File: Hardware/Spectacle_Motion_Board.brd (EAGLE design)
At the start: 25.4 x 55.9 mm, 49 parts, among them J10 AUDIO-JACK3, J3 USB-MICROB, J4 AUDIO-JACK3, U1 CY8C4146LQI-S422, U2 3.3V/150mA, U4 SN74LVC1G66, U5 SN74LVC1G66

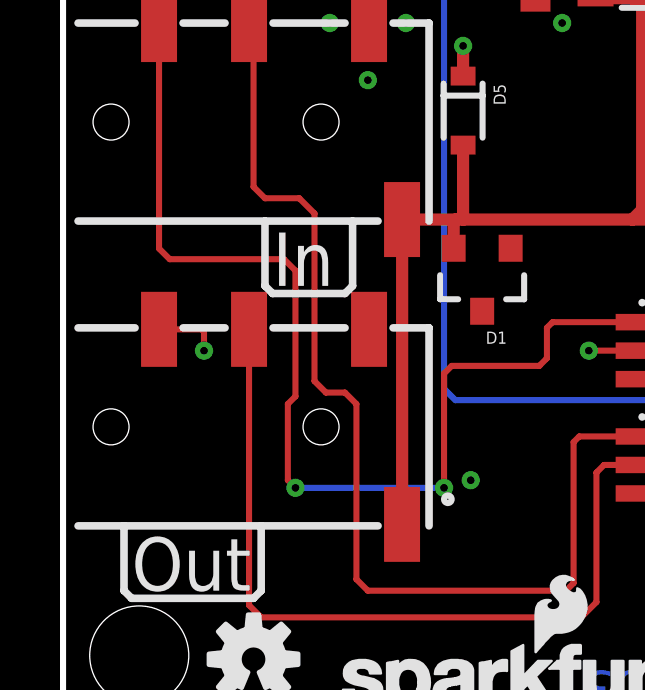
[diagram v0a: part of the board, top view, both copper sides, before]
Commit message: Added and fixed some product IDs
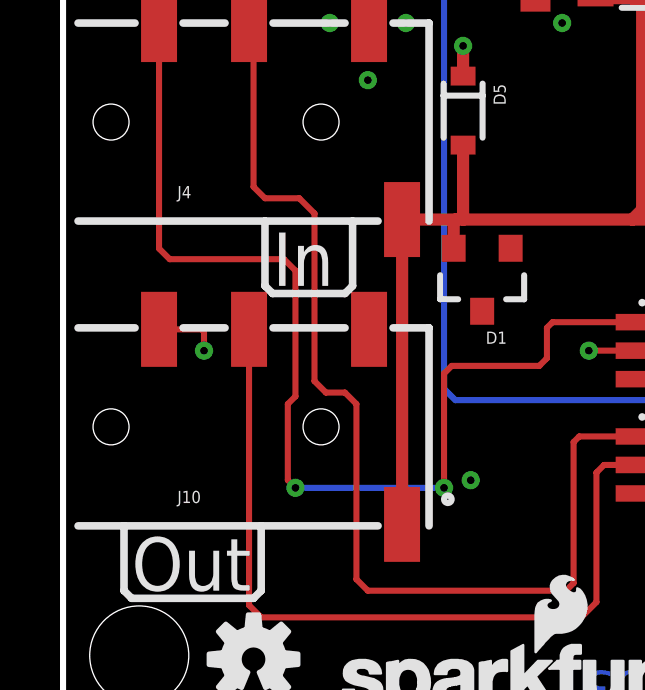
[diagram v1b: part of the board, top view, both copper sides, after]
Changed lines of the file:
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@@
 <grid distance="0.05" unitdist="inch" unit="inch" style="lines" multiple="1" display="yes" altdistance="0.005" altunitdist="inch" altunit="inch"/>
 <layers>
-<layer number="1" name="Top" color="4" fill="1" visible="no" active="yes"/>
+<layer number="1" name="Top" color="4" fill="1" visible="yes" active="yes"/>
 <layer number="2" name="Route2" color="1" fill="3" visible="no" active="yes"/>
-<layer number="15" name="Route15" color="4" fill="6" visible="yes" active="yes"/>
-<layer number="16" name="Bottom" color="1" fill="1" visible="no" active="yes"/>
+<layer number="15" name="Route15" color="4" fill="6" visible="no" active="yes"/>
+<layer number="16" name="Bottom" color="1" fill="1" visible="yes" active="yes"/>
 <layer number="17" name="Pads" color="2" fill="1" visible="yes" active="yes"/>
 <layer number="18" name="Vias" color="2" fill="1" visible="yes" active="yes"/>
 <layer number="19" name="Unrouted" color="6" fill="1" visible="yes" active="yes"/>
 <layer number="20" name="Dimension" color="15" fill="1" visible="yes" active="yes"/>
-<layer number="21" name="tPlace" color="16" fill="1" visible="no" active="yes"/>
-<layer number="22" name="bPlace" color="14" fill="1" visible="no" active="yes"/>
-<layer number="23" name="tOrigins" color="15" fill="1" visible="no" active="yes"/>
-<layer number="24" name="bOrigins" color="15" fill="1" visible="no" active="yes"/>
+<layer number="21" name="tPlace" color="16" fill="1" visible="yes" active="yes"/>
+<layer number="22" name="bPlace" color="14" fill="1" visible="yes" active="yes"/>
+<layer number="23" name="tOrigins" color="15" fill="1" visible="yes" active="yes"/>
+<layer number="24" name="bOrigins" color="15" fill="1" visible="yes" active="yes"/>
 <layer number="25" name="tNames" color="7" fill="1" visible="no" active="yes"/>
 <layer number="26" name="bNames" color="7" fill="1" visible="no" active="yes"/>
@@
 <layer number="43" name="vRestrict" color="2" fill="10" visible="no" active="yes"/>
 <layer number="44" name="Drills" color="7" fill="1" visible="no" active="yes"/>
-<layer number="45" name="Holes" color="7" fill="1" visible="no" active="yes"/>
+<layer number="45" name="Holes" color="7" fill="1" visible="yes" active="yes"/>
 <layer number="46" name="Milling" color="3" fill="1" visible="no" active="yes"/>
 <layer number="47" name="Measures" color="7" fill="1" visible="no" active="yes"/>
 <layer number="48" name="Document" color="7" fill="1" visible="no" active="yes"/>
 <layer number="49" name="Reference" color="7" fill="1" visible="no" active="yes"/>
-<layer number="51" name="tDocu" color="6" fill="1" visible="no" active="yes"/>
+<layer number="51" name="tDocu" color="6" fill="1" visible="yes" active="yes"/>
 <layer number="52" name="bDocu" color="7" fill="1" visible="no" active="yes"/>
 <layer number="3" name="Route3" color="4" fill="3" visible="no" active="no"/>
@@
 <element name="H3" library="SparkFun-Electromechanical" package="STAND-OFF" value="STAND-OFF" x="22.86" y="2.54"/>
 <element name="H4" library="SparkFun-Electromechanical" package="STAND-OFF" value="STAND-OFF" x="2.54" y="2.54"/>
-<element name="J3" library="SparkFun-Connectors" package="USB-B-MICRO-SMD_V03_RED_PASTE" value="USB-MICROB" x="12.7" y="53.848" rot="R270"/>
-<element name="J5" library="SparkFun-Connectors" package="1X03_LOCK" value="" x="6.35" y="41.91" rot="R90"/>
-<element name="J6" library="SparkFun-Connectors" package="1X03_LOCK" value="" x="9.525" y="41.91" rot="R90"/>
-<element name="J7" library="SparkFun-Connectors" package="1X03_LOCK" value="" x="12.7" y="41.91" rot="R90"/>
-<element name="J8" library="SparkFun-Connectors" package="1X03_LOCK" value="" x="15.875" y="41.91" rot="R90"/>
-<element name="J9" library="SparkFun-Connectors" package="1X03_LOCK" value="" x="19.05" y="41.91" rot="R90"/>
+<element name="J3" library="SparkFun-Connectors" package="USB-B-MICRO-SMD_V03_RED_PASTE" value="USB-MICROB" x="12.7" y="53.848" rot="R270">
+<attribute name="PROD_ID" value="CONN-11752" x="12.7" y="53.848" size="1.778" layer="27" rot="R270" display="off"/>
+</element>
+<element name="J5" library="SparkFun-Connectors" package="1X03_LOCK" value="" x="6.35" y="41.91" rot="R90">
+<attribute name="PROD_ID" value="CONN-09692" x="6.35" y="41.91" size="1.778" layer="27" rot="R90" display="off"/>
+</element>
+<element name="J6" library="SparkFun-Connectors" package="1X03_LOCK" value="" x="9.525" y="41.91" rot="R90">
+<attribute name="PROD_ID" value="CONN-09692" x="9.525" y="41.91" size="1.778" layer="27" rot="R90" display="off"/>
+</element>
+<element name="J7" library="SparkFun-Connectors" package="1X03_LOCK" value="" x="12.7" y="41.91" rot="R90">
+<attribute name="PROD_ID" value="CONN-09692" x="12.7" y="41.91" size="1.778" layer="27" rot="R90" display="off"/>
+</element>
+<element name="J8" library="SparkFun-Connectors" package="1X03_LOCK" value="" x="15.875" y="41.91" rot="R90">
+<attribute name="PROD_ID" value="CONN-09692" x="15.875" y="41.91" size="1.778" layer="27" rot="R90" display="off"/>
+</element>
+<element name="J9" library="SparkFun-Connectors" package="1X03_LOCK" value="" x="19.05" y="41.91" rot="R90">
+<attribute name="PROD_ID" value="CONN-09692" x="19.05" y="41.91" size="1.778" layer="27" rot="R90" display="off"/>
+</element>
 <element name="U$1" library="SparkFun-Aesthetics" package="FOUR_LAYER_WARNING" value="FOUR_LAYER_WARNING" x="39.37" y="54.61"/>
 <element name="LOGO1" library="SparkFun-Aesthetics" package="OSHW-LOGO-S" value="OSHW-LOGOS" x="6.35" y="2.413"/>
@@
 <attribute name="PROD_ID" value="DIO-11623" x="13.335" y="20.701" size="1.778" layer="27" font="vector" ratio="15" rot="R270" display="off"/>
 </element>
-<element name="J11" library="SparkFun-Connectors" package="1X06_NO_SILK" value="" x="1.27" y="43.18" rot="R270">
-<attribute name="PROD_ID" value="CONN-08437" x="1.27" y="43.18" size="1.778" layer="27" font="vector" ratio="15" rot="R270" display="off"/>
-</element>
+<element name="J11" library="SparkFun-Connectors" package="1X06_NO_SILK" value="" x="1.27" y="43.18" rot="R270"/>
 <element name="U4" library="SparkFun-AnalogIC" package="SOT23-5" value="SN74LVC1G66" x="20.32" y="12.7" rot="R270">
 <attribute name="PROD_ID" value="IC-13549" x="25.4" y="17.78" size="1.778" layer="27" font="vector" ratio="15" rot="R270" display="off"/>

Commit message: Touchups for v10
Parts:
- J10, J4: value AUDIO-JACK3 -> TRRS_3.5mm; device SparkFun-Connectors:AUDIO-JACK-TRRS-SMD -> SparkFun-Connectors:AUDIO_JACK_3.5MM_TRRS_SMD_RA
- moved LOGO3 18.7 mm to (19.4, 5.71)
- moved LOGO4 1.27 mm to (2.16, 46.6)
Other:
- board text added: "v10"
- board text removed: "v03"
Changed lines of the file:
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@@
 <?xml version="1.0" encoding="utf-8"?>
 <!DOCTYPE eagle SYSTEM "eagle.dtd">
-<eagle version="7.6.0">
+<eagle version="7.7.0">
 <drawing>
 <settings>
@@
 <grid distance="0.05" unitdist="inch" unit="inch" style="lines" multiple="1" display="yes" altdistance="0.005" altunitdist="inch" altunit="inch"/>
 <layers>
-<layer number="1" name="Top" color="4" fill="1" visible="yes" active="yes"/>
+<layer number="1" name="Top" color="4" fill="1" visible="no" active="yes"/>
 <layer number="2" name="Route2" color="1" fill="3" visible="no" active="yes"/>
 <layer number="15" name="Route15" color="4" fill="6" visible="no" active="yes"/>
@@
 <layer number="19" name="Unrouted" color="6" fill="1" visible="yes" active="yes"/>
 <layer number="20" name="Dimension" color="15" fill="1" visible="yes" active="yes"/>
-<layer number="21" name="tPlace" color="16" fill="1" visible="yes" active="yes"/>
+<layer number="21" name="tPlace" color="16" fill="1" visible="no" active="yes"/>
 <layer number="22" name="bPlace" color="14" fill="1" visible="yes" active="yes"/>
-<layer number="23" name="tOrigins" color="15" fill="1" visible="yes" active="yes"/>
+<layer number="23" name="tOrigins" color="15" fill="1" visible="no" active="yes"/>
 <layer number="24" name="bOrigins" color="15" fill="1" visible="yes" active="yes"/>
 <layer number="25" name="tNames" color="7" fill="1" visible="no" active="yes"/>
@@
 <layer number="43" name="vRestrict" color="2" fill="10" visible="no" active="yes"/>
 <layer number="44" name="Drills" color="7" fill="1" visible="no" active="yes"/>
-<layer number="45" name="Holes" color="7" fill="1" visible="yes" active="yes"/>
+<layer number="45" name="Holes" color="7" fill="1" visible="no" active="yes"/>
 <layer number="46" name="Milling" color="3" fill="1" visible="no" active="yes"/>
 <layer number="47" name="Measures" color="7" fill="1" visible="no" active="yes"/>
 <layer number="48" name="Document" color="7" fill="1" visible="no" active="yes"/>
 <layer number="49" name="Reference" color="7" fill="1" visible="no" active="yes"/>
-<layer number="51" name="tDocu" color="6" fill="1" visible="yes" active="yes"/>
+<layer number="51" name="tDocu" color="6" fill="1" visible="no" active="yes"/>
 <layer number="52" name="bDocu" color="7" fill="1" visible="no" active="yes"/>
 <layer number="3" name="Route3" color="4" fill="3" visible="no" active="no"/>
@@
 <text x="19.177" y="49.149" size="1.4224" layer="21" font="vector" ratio="15" align="center">4</text>
 <text x="90.17" y="45.72" size="1.778" layer="51" font="vector" ratio="15">Mike Hord</text>
-<text x="20.32" y="0.762" size="1.27" layer="16" font="vector" ratio="15" rot="MR0">v03</text>
+<text x="20.32" y="0.762" size="1.27" layer="16" font="vector" ratio="15" rot="MR0">v10</text>
 <text x="0.635" y="50.038" size="1.27" layer="1" font="vector" ratio="15">1</text>
 <text x="1.778" y="50.038" size="1.27" layer="2" font="vector" ratio="15">2</text>
@@
 <wire x1="9.398" y1="14.605" x2="9.652" y2="14.859" width="0.254" layer="21"/>
 <wire x1="9.652" y1="14.859" x2="9.652" y2="17.018" width="0.254" layer="21"/>
-<circle x="12.827" y="7.747" radius="0.127" width="0.2032" layer="21"/>
 </plain>
 <attributes>
@@
 <attribute name="PROD_ID" value="RES-07856" x="19.05" y="30.48" size="1.778" layer="27" font="vector" ratio="15" rot="R180" display="off"/>
 </element>
-<element name="J4" library="SparkFun-Connectors" package="AUDIO-JACK-TRRS-SMD" value="AUDIO-JACK3" x="0" y="20.32">
+<element name="J4" library="SparkFun-Connectors" package="AUDIO_JACK_3.5MM_TRRS_SMD_RA" value="TRRS_3.5mm" x="0" y="20.32">
 <attribute name="PROD_ID" value="CONN-10676" x="0" y="20.32" size="1.778" layer="27" display="off"/>
+<attribute name="SF_ID" value="PRT-12639" x="0" y="20.32" size="1.778" layer="27" display="off"/>
 </element>
 <element name="D4" library="SparkFun-DiscreteSemi" package="SOT23-3" value="PESD1CAN" x="4.699" y="27.178">
@@
 <element name="LOGO1" library="SparkFun-Aesthetics" package="OSHW-LOGO-S" value="OSHW-LOGOS" x="6.35" y="2.413"/>
 <element name="LOGO2" library="SparkFun-Aesthetics" package="SFE_LOGO_NAME_FLAME_.1" value="SFE_LOGO_NAME_FLAME.1_INCH" x="8.89" y="0"/>
-<element name="J10" library="SparkFun-Connectors" package="AUDIO-JACK-TRRS-SMD" value="AUDIO-JACK3" x="0" y="10.16">
+<element name="J10" library="SparkFun-Connectors" package="AUDIO_JACK_3.5MM_TRRS_SMD_RA" value="TRRS_3.5mm" x="0" y="10.16">
 <attribute name="PROD_ID" value="CONN-10676" x="0" y="10.16" size="1.778" layer="27" display="off"/>
-</element>
-<element name="LOGO3" library="SparkFun-Aesthetics" package="SFE_LOGO_NAME_FLAME_.1" value="SFE_LOGO_NAME_FLAME.1_INCH" x="0.762" y="4.445" rot="MR90"/>
-<element name="LOGO4" library="SparkFun-Aesthetics" package="OSHW-LOGO-S" value="OSHW-LOGOS" x="2.159" y="47.879" rot="MR90"/>
+<attribute name="SF_ID" value="PRT-12639" x="0" y="10.16" size="1.778" layer="27" display="off"/>
+</element>
+<element name="LOGO3" library="SparkFun-Aesthetics" package="SFE_LOGO_NAME_FLAME_.1" value="SFE_LOGO_NAME_FLAME.1_INCH" x="19.431" y="5.715" rot="MR90"/>
+<element name="LOGO4" library="SparkFun-Aesthetics" package="OSHW-LOGO-S" value="OSHW-LOGOS" x="2.159" y="46.609" rot="MR90"/>
 <element name="U$3" library="SparkFun-Aesthetics" package="SPECTACLE_LOGO_NEGATIVE_1.5X0.5" value="" x="6.35" y="2.54" rot="MR90"/>
 <element name="FD1" library="SparkFun-Aesthetics" package="MICRO-FIDUCIAL" value="FIDUCIALUFIDUCIAL" x="20.32" y="3.81"/>
